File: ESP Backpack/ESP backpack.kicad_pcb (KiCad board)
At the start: 2 copper layers, 100 x 100 mm, 37 parts, among them J1 HLE-120-02-F-DV-BE-K, J2 HLE-120-02-F-DV-BE-K, U1 ESP32-DEVKITC-32D, U2 VCNL4010-GS08

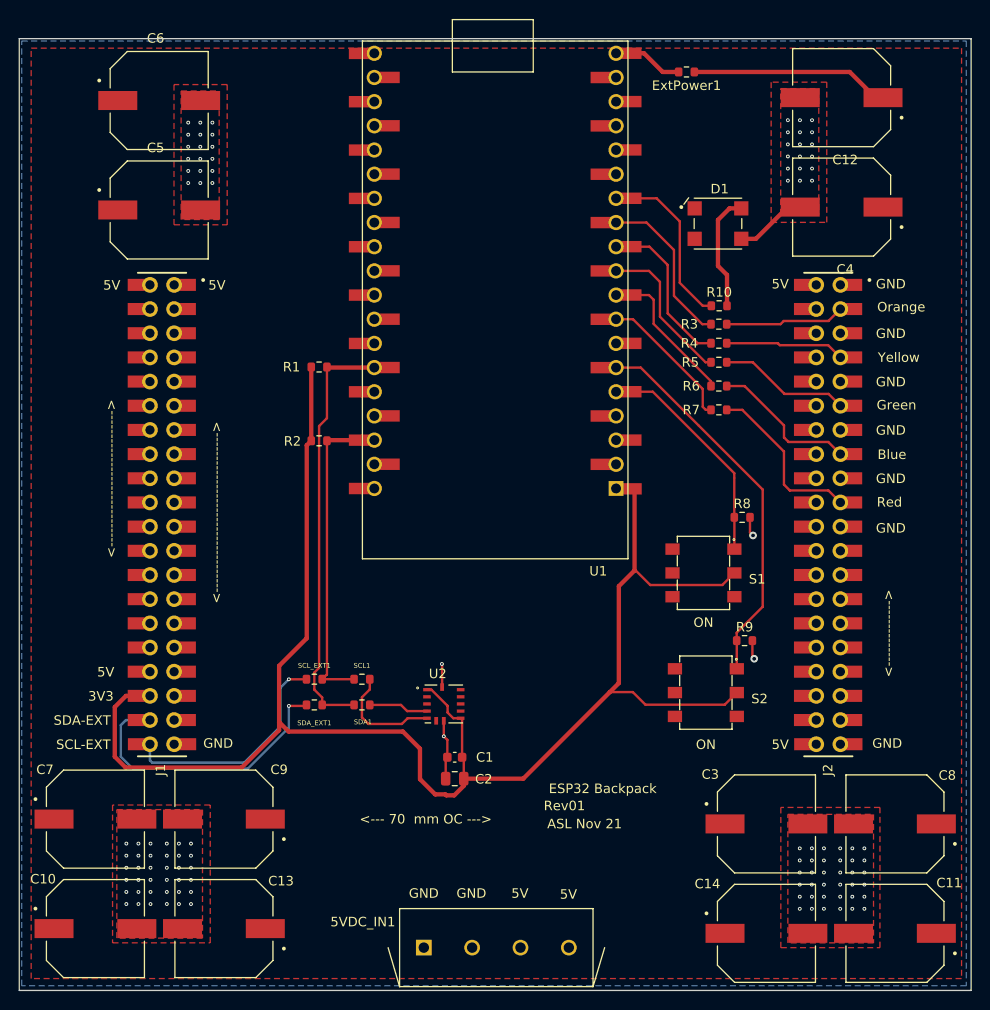
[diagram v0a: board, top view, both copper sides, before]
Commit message: edit all libs and footprints into single libraries and files. Issue fixes
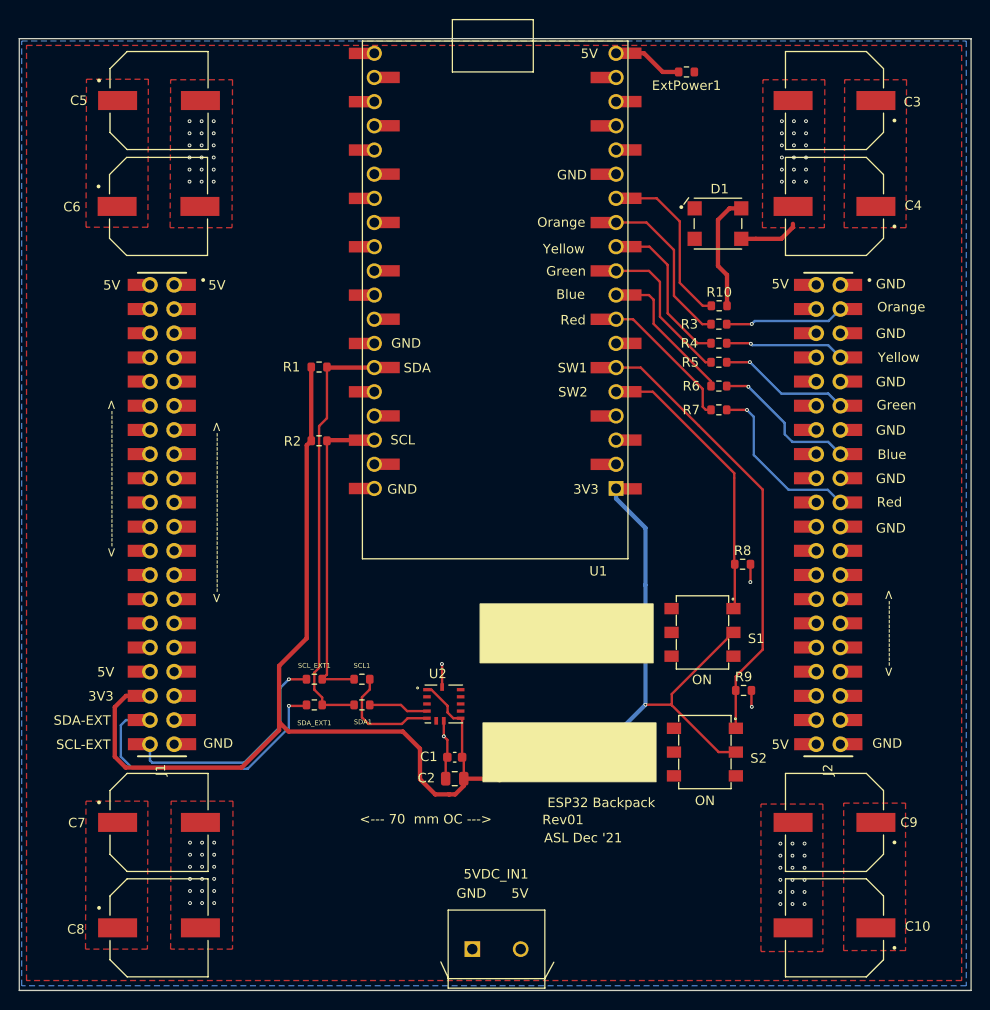
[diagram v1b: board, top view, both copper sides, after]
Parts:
- removed C11, C12, C13, C14: EEE0JA102P, Custom Libraries:CAP_EEE0JA102P
- 5VDC_IN1: value 282837-4 -> 282837-2; footprint Custom Libraries:TE_282837-4 -> _ESP-Backpack-Custom-Libraries:TE_282837-2
- C10, C3, C4, C5, C6, C7, C8, C9: value EEE0JA102P -> A765MU158M1ALAE014; footprint Custom Libraries:CAP_EEE0JA102P -> _ESP-Backpack-Custom-Libraries:CAP_EEE0JA102P
- moved C8 78.1 mm to (14.7, 93.4), turned to 0 degrees
- moved C10 77.6 mm to (85.6, 93.4), turned to 180 degrees
- moved C3 76.3 mm to (85.6, 6.50), turned to 180 degrees
- moved C9 64.1 mm to (85.6, 82.3)
- moved C5 11.5 mm to (14.7, 6.50)
- moved C6 11.1 mm to (14.6, 17.6)
- moved 5VDC_IN1 7.64 mm to (50.1, 95.7)
- moved C7 6.69 mm to (14.7, 82.3)
- moved S2 6.25 mm to (72.0, 75.0)
- moved S1 6.25 mm to (71.8, 62.4)
- moved R9 5.23 mm to (76.1, 68.5)
- moved R8 4.93 mm to (76.0, 55.2)
- moved C4 0.75 mm to (85.6, 17.6)
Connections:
- 5VDC_IN1 pad 2: GND -> +5V
- D1 pad 2: (no net) -> Net-(D1-Pad2)
- S1 pad 3: (no net) -> Net-(S1-Pad3)
- S1 pad 4: (no net) -> Net-(S1-Pad4)
- S1 pad 5: (no net) -> Net-(S1-Pad5)
- S1 pad 6: (no net) -> Net-(S1-Pad6)
- S2 pad 3: (no net) -> Net-(S2-Pad3)
- S2 pad 4: (no net) -> Net-(S2-Pad4)
- S2 pad 5: (no net) -> Net-(S2-Pad5)
- S2 pad 6: (no net) -> Net-(S2-Pad6)
- U2 pad 10: (no net) -> Net-(U2-Pad10)
- U2 pad 11: (no net) -> Net-(U2-Pad11)
- U2 pad 2: (no net) -> Net-(U2-Pad2)
- U2 pad 3: (no net) -> Net-(U2-Pad3)
- U2 pad 6: (no net) -> Net-(U2-Pad6)
- U2 pad 8: (no net) -> Net-(U2-Pad8)
- U2 pad 9: (no net) -> Net-(U2-Pad9)
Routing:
- net +5V: track 21.3 -> 1.19 mm
- net Net-(R8-Pad1): track 22.3 -> 28.7 mm
- net Net-(R9-Pad1): track 42.3 -> 48.6 mm
- net GND: track 30.2 -> 28.5 mm, vias 112 -> 76
- net +3V3: track 172.2 -> 172.9 mm, vias 0 -> 2
- net /RedLine: track 19.4 -> 19.7 mm, vias 0 -> 1
- net /BlueLine: vias 0 -> 1
- net /GreenLine: track 15.2 -> 15.3 mm, vias 0 -> 1
- net /OrangeLine: vias 0 -> 1
- net /YellowLine: vias 0 -> 1
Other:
- board text added: "ASL Dec '21"
- board text added: "SCL"
- board text added: "SDA"
- board text added: "SW1"
- board text added: "SW2"
- board text removed: "ASL Nov 21"
